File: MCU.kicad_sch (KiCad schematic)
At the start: 46 parts, among them J1 CC Prog/Debug, J2 UART0, J7 Control Outputs, U1 CC1110, U2 MIC803, X1 TG2520SMN 27MHz

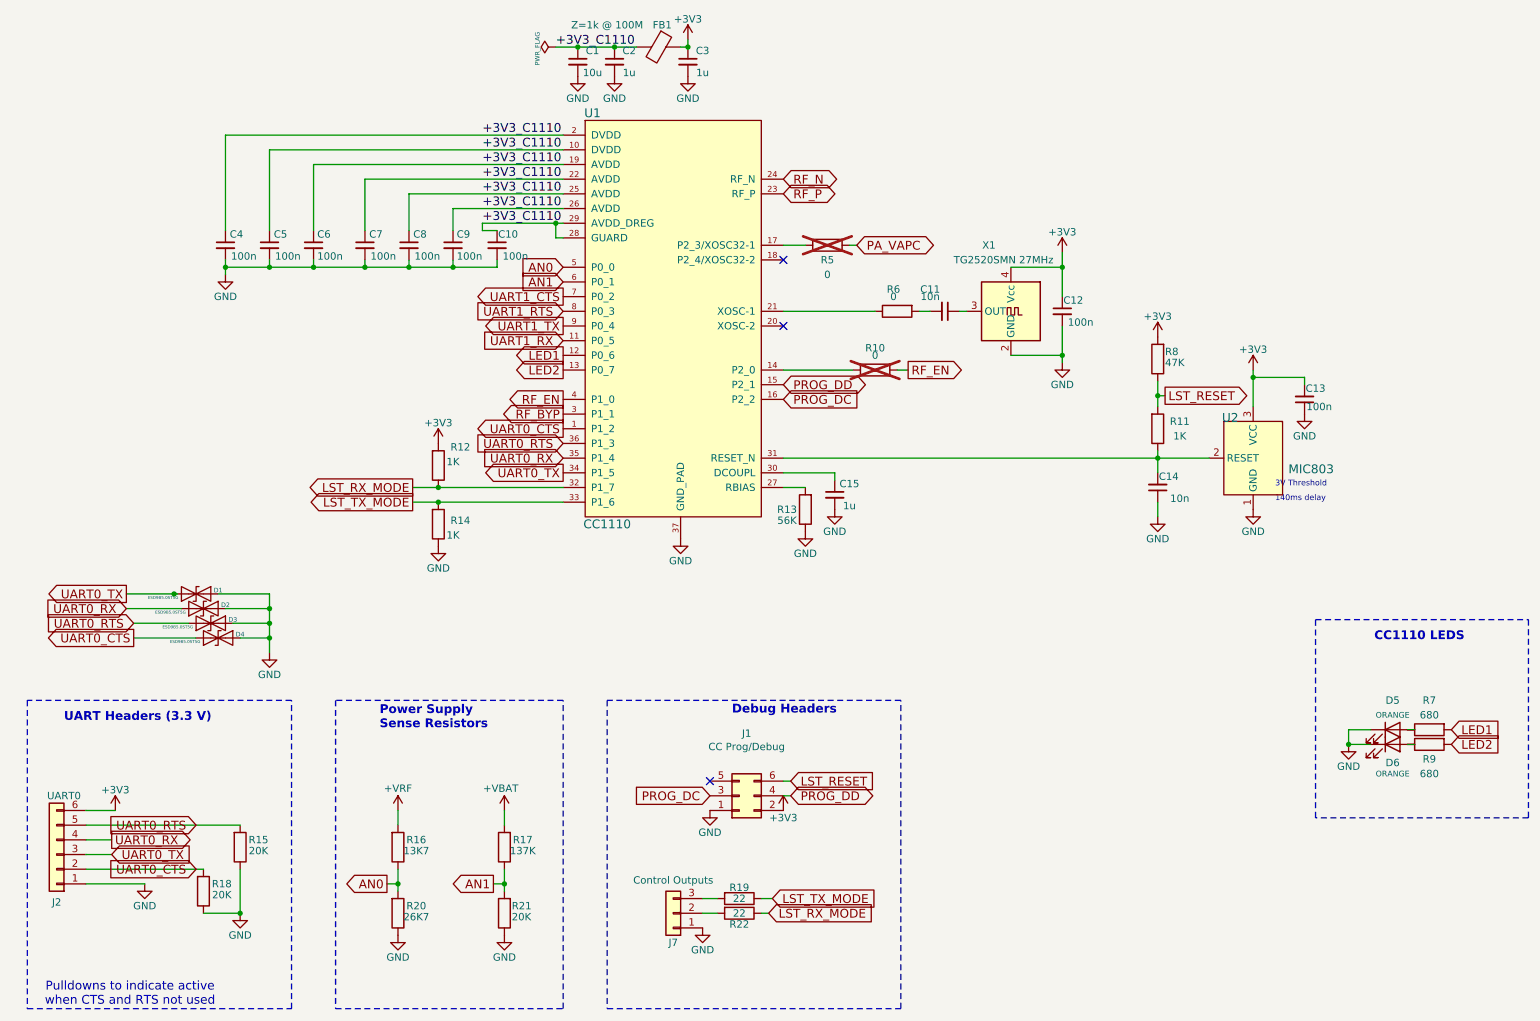
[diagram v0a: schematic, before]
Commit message: automatic schematic and pcb valiadation and cleanup
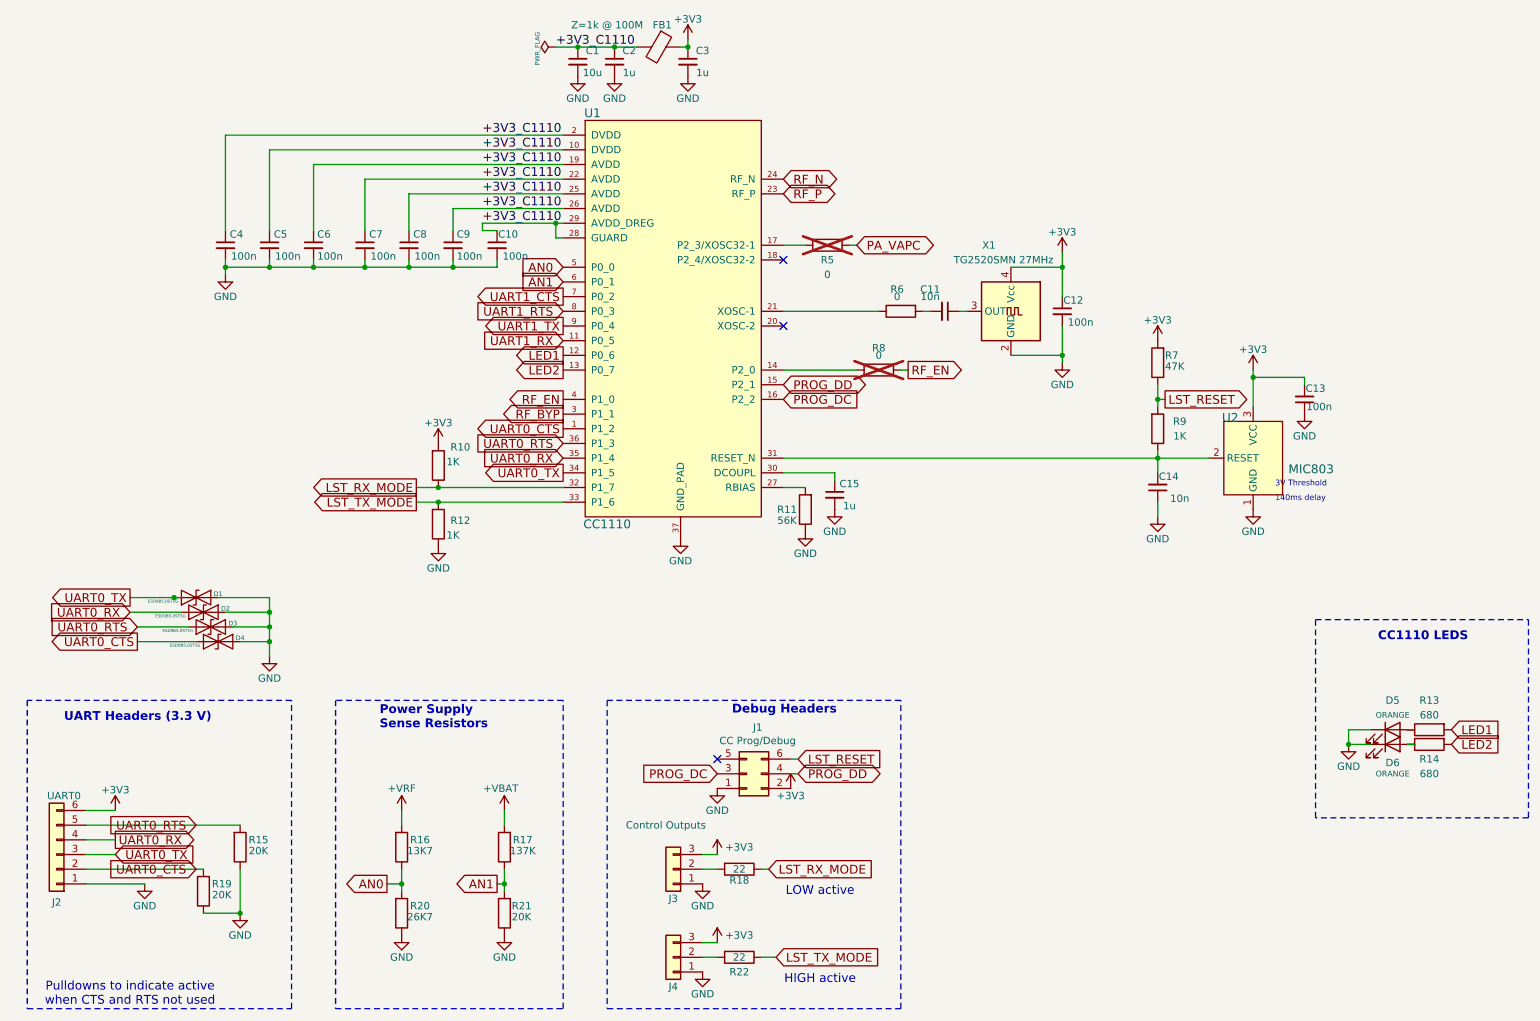
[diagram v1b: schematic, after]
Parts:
- removed R19: 22, Resistor_SMD:R_0603_1608Metric_Pad0.98x0.95mm_HandSolder, symbol Device:R
- added J4: Control Outputs, Connector_PinHeader_2.54mm:PinHeader_1x03_P2.54mm_Vertical, symbol Connector_Generic:Conn_01x03
- added R22: 22, Resistor_SMD:R_0603_1608Metric_Pad0.98x0.95mm_HandSolder, symbol Device:R
- renumbered J7 to J3, R12 to R10, R13 to R11, R14 to R12, R7 to R13, R9 to R14, R22 to R18, R18 to R19, R8 to R7, R10 to R8, R11 to R9
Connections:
- net +3V3: now also J3.3 (Pin_3), J4.3 (Pin_3)
- net GND: now also J4.1 (Pin_1)
- net LST_TX_MODE: now also R22.1
- new net: J4.2 (Pin_2), R22.2
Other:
- note added: "HIGH active"
- note added: "LOW active"
- moved on the sheet: D1, D2, D3, D4, J1, J3, R16, R18, R20, R6, R7, R8

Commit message: temporary branch for radio to pc104
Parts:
- removed D1, D2, D3, D4: ESD9B5.0ST5G, LED_SMD:LED_0603_1608Metric_Pad1.05x0.95mm_HandSolder, symbol Diode:ESD9B5.0ST5G
- added TP1: TestPoint, symbol Connector:TestPoint
- R11: renamed from R15; value 20K -> 100K
- R12: renamed from R16; value 13K7 -> DNP; now not fitted
- R13: renamed from R17; value 137K -> 20K
- R15: renamed from R19; value 20K -> 100K
- R16: renamed from R20; value 26K7 -> DNP; now not fitted
- R17: renamed from R21; value 20K -> 47K
- renumbered D5 to D1, D6 to D2, R5 to R1, R14 to R10, R18 to R14, R22 to R18, R6 to R2, R7 to R3, R8 to R4, R9 to R5, R10 to R6, R11 to R7, R12 to R8, R13 to R9
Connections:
- net UART0_CTS: no longer J2.2 (Pin_2), R15.2
- net UART0_RTS: no longer J2.5 (Pin_5), R11.2
- net UART0_RX: no longer J2.4 (Pin_4)
- net UART0_TX: no longer J2.3 (Pin_3)
- net UART1_CTS: now also J2.2 (Pin_2), R15.2
- net UART1_RTS: now also J2.5 (Pin_5), R11.2
- net UART1_RX: now also J2.4 (Pin_4)
- net UART1_TX: now also J2.3 (Pin_3)
- net +3V3 renamed 3V3
- net +VBAT renamed VRF
- net +VRF: no longer names the net of R12.2
- net +VRF: now also TP1.1
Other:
- moved on the sheet: C3

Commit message: use Common libraries, replace TI MCU with STM32 for CAN bridge
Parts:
- TP1: footprint (none) -> TestPoint:TestPoint_Pad_1.5x1.5mm
- U1: footprint Project:Texas_RHH0036C_VQFN-36-1EP_6x6mm_P0.5mm_EP4.4x4.4mm_ThermalVias -> Common:Texas_RHH0036C_VQFN-36-1EP_6x6mm_P0.5mm_EP4.4x4.4mm_ThermalVias
- X1: value TG2520SMN 27MHz -> 27MHz; footprint Project:Oscillator_SMD_SeikoEpson_TG2520SMN-xxx-xxxxxx-4Pin_2.5x2.0mm -> Oscillator:Oscillator_SMD_Abracon_ASDMB-4Pin_2.5x2.0mm; Mfr. # TG2520SMN 27.0000M-MCGNNM3 -> ASDAIG-27.000MHZ-C-S-T
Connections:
- net UART0_CTS: now also J2.2 (Pin_2), R15.2
- net UART0_RTS: now also J2.5 (Pin_5), R11.2
- net UART0_RX: now also J2.4 (Pin_4)
- net UART0_TX: now also J2.3 (Pin_3)
- net UART1_CTS: no longer J2.2 (Pin_2), R15.2
- net UART1_RTS: no longer J2.5 (Pin_5), R11.2
- net UART1_RX: no longer J2.4 (Pin_4)
- net UART1_TX: no longer J2.3 (Pin_3)
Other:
- note added: "UART0 Headers (3.3 V)"
- note removed: "UART Headers (3.3 V)"
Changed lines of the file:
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@@
 		)
 	)
-	(text "UART Headers (3.3 V)"
+	(text "UART0 Headers (3.3 V)"
 		(exclude_from_sim no)
 		(at 27.94 146.05 0)
@@
 		)
 	)
-	(label "UART1_TX"
-		(at 114.3 77.47 180)
-		(fields_autoplaced yes)
-		(effects
-			(font
-				(size 1.524 1.524)
-			)
-			(justify right bottom)
-		)
-	)
 	(label "+3V3_C1110"
 		(at 114.3 59.69 180)
@@
 		)
 	)
-	(label "UART1_CTS"
+	(label "UART0_CTS"
 		(at 50.8 171.45 180)
 		(fields_autoplaced yes)
@@
 		)
 	)
-	(label "UART1_RX"
+	(label "UART0_RX"
 		(at 38.1 166.37 0)
 		(fields_autoplaced yes)
@@
 		)
 	)
-	(label "UART1_RTS"
-		(at 114.3 74.93 180)
+	(label "LED1"
+		(at 114.3 82.55 180)
 		(fields_autoplaced yes)
 		(effects
@@
 		)
 	)
-	(label "LED1"
-		(at 114.3 82.55 180)
+	(label "+3V3_C1110"
+		(at 113.03 29.21 0)
 		(fields_autoplaced yes)
 		(effects
@@
 				(size 1.524 1.524)
 			)
-			(justify right bottom)
+			(justify left bottom)
 		)
 	)
-	(label "UART1_RX"
-		(at 114.3 80.01 180)
+	(label "UART0_RX"
+		(at 114.3 100.33 180)
 		(fields_autoplaced yes)
 		(effects
@@
 		)
 	)
-	(label "+3V3_C1110"
-		(at 113.03 29.21 0)
+	(label "LST_TX_MODE"
+		(at 151.13 186.69 0)
 		(fields_autoplaced yes)
 		(effects
@@
 		)
 	)
-	(label "LST_TX_MODE"
-		(at 151.13 186.69 0)
+	(label "+3V3_C1110"
+		(at 99.695 46.99 0)
 		(fields_autoplaced yes)
 		(effects
@@
 		)
 	)
-	(label "+3V3_C1110"
-		(at 99.695 46.99 0)
+	(label "UART0_CTS"
+		(at 114.3 95.25 180)
 		(fields_autoplaced yes)
 		(effects
@@
 				(size 1.524 1.524)
 			)
-			(justify left bottom)
+			(justify right bottom)
 		)
 	)
-	(label "UART1_TX"
+	(label "UART0_TX"
 		(at 38.1 168.91 0)
 		(fields_autoplaced yes)
@@
 		)
 	)
-	(label "UART1_RTS"
+	(label "UART0_RTS"
 		(at 50.8 163.83 180)
 		(fields_autoplaced yes)
@@
 		)
 	)
-	(label "UART1_CTS"
-		(at 114.3 72.39 180)
+	(label "UART0_RTS"
+		(at 114.3 97.79 180)
+		(fields_autoplaced yes)
+		(effects
+			(font
+				(size 1.524 1.524)
+			)
+			(justify right bottom)
+		)
+	)
+	(label "UART0_TX"
+		(at 114.3 102.87 180)
 		(fields_autoplaced yes)
 		(effects
@@
 		)
 	)
-	(hierarchical_label "UART0_TX"
-		(shape output)
-		(at 114.3 102.87 180)
-		(fields_autoplaced yes)
-		(effects
-			(font
-				(size 1.524 1.524)
-			)
-			(justify right)
-		)
-	)
 	(hierarchical_label "3V3"
 		(shape input)
@@
 		)
 	)
-	(hierarchical_label "UART0_CTS"
-		(shape output)
-		(at 114.3 95.25 180)
-		(fields_autoplaced yes)
-		(effects
-			(font
-				(size 1.524 1.524)
-			)
-			(justify right)
-		)
-	)
 	(hierarchical_label "LST_RX_MODE"
 		(shape output)
@@
 		)
 	)
-	(hierarchical_label "UART0_RX"
-		(shape input)
-		(at 114.3 100.33 180)
-		(fields_autoplaced yes)
-		(effects
-			(font
-				(size 1.524 1.524)
-			)
-			(justify right)
-		)
-	)
 	(hierarchical_label "VRF"
 		(shape input)
@@
 		)
 	)
-	(hierarchical_label "GND"
+	(hierarchical_label "UART1_TX"
 		(shape input)
-		(at 233.68 110.49 0)
+		(at 114.3 77.47 180)
 		(fields_autoplaced yes)
 		(effects
@@
 				(size 1.524 1.524)
 			)
-			(justify left)
+			(justify right)
 		)
 	)
-	(hierarchical_label "UART0_RTS"
+	(hierarchical_label "GND"
 		(shape input)
-		(at 114.3 97.79 180)
+		(at 233.68 110.49 0)
 		(fields_autoplaced yes)
 		(effects
@@
 				(size 1.524 1.524)
 			)
-			(justify right)
+			(justify left)
 		)
 	)
@@
 		)
 	)
+	(hierarchical_label "UART1_RTS"
+		(shape input)
+		(at 114.3 74.93 180)
+		(fields_autoplaced yes)
+		(effects
+			(font
+				(size 1.524 1.524)
+			)
+			(justify right)
+		)
+	)
 	(hierarchical_label "3V3"
 		(shape input)
@@
 		)
 	)
+	(hierarchical_label "UART1_RX"
+		(shape input)
+		(at 114.3 80.01 180)
+		(fields_autoplaced yes)
+		(effects
+			(font
+				(size 1.524 1.524)
+			)
+			(justify right)
+		)
+	)
 	(hierarchical_label "3V3"
 		(shape input)
@@
 		)
 	)
+	(hierarchical_label "UART1_CTS"
+		(shape input)
+		(at 114.3 72.39 180)
+		(fields_autoplaced yes)
+		(effects
+			(font
+				(size 1.524 1.524)
+			)
+			(justify right)
+		)
+	)
 	(hierarchical_label "RF_EN"
 		(shape output)
@@
 			)
 		)
-		(property "Value" "TG2520SMN 27MHz"
+		(property "Value" "27MHz"
 			(at 190.5 66.04 0)
 			(effects
@@
 			)
 		)
-		(property "Footprint" "Project:Oscillator_SMD_SeikoEpson_TG2520SMN-xxx-xxxxxx-4Pin_2.5x2.0mm"
+		(property "Footprint" "Oscillator:Oscillator_SMD_Abracon_ASDMB-4Pin_2.5x2.0mm"
 			(at 180.34 83.82 0)
 			(effects
@@
 			)
 		)
-		(property "Datasheet" "https://support.epson.biz/td/api/doc_check.php?dl=app_TG2520SMN&lang=en"
+		(property "Datasheet" "https://abracon.com/AIGOscillators/ASDAIG.pdf"
 			(at 194.31 74.93 0)
 			(effects
@@
 			)
 		)
-		(property "Description" "Crystal Oscillator Low Profile / High Stability TCXO"
+		(property "Description" "Crystal Oscillator 27MHz"
 			(at 191.77 74.93 0)
 			(effects
@@
 			)
 		)
-		(property "Mfr. #" "TG2520SMN 27.0000M-MCGNNM3"
+		(property "Mfr. #" "ASDAIG-27.000MHZ-C-S-T"
 			(at 191.77 66.6496 0)
 			(effects
@@
 			)
 		)
-		(property "Footprint" "Project:Texas_RHH0036C_VQFN-36-1EP_6x6mm_P0.5mm_EP4.4x4.4mm_ThermalVias"
+		(property "Footprint" "Common:Texas_RHH0036C_VQFN-36-1EP_6x6mm_P0.5mm_EP4.4x4.4mm_ThermalVias"
 			(at 138.43 90.17 0)
 			(effects
@@
 		(on_board yes)
 		(dnp no)
-		(property "Reference" "#FLG01"
+		(property "Reference" "#FLG05"
 			(at 111.125 29.21 0)
 			(effects
@@
 			(project "openlst-hw"
 				(path "/a863a5ec-a5d4-4f54-be53-e8c01d5e3ac4/f5534efb-fc6e-465a-a57b-daca63f2ce0c"
-					(reference "#FLG01")
+					(reference "#FLG05")
 					(unit 1)
 				)
@@
 			)
 		)
-		(property "Footprint" ""
+		(property "Footprint" "TestPoint:TestPoint_Pad_1.5x1.5mm"
 			(at 91.44 161.29 0)
 			(effects
@@
 		(on_board yes)
 		(dnp no)
-		(property "Reference" "#PWR06"
+		(property "Reference" "#PWR02"
 			(at 250.19 156.21 0)
 			(effects
@@
 			(project "openlst-hw"
 				(path "/a863a5ec-a5d4-4f54-be53-e8c01d5e3ac4/f5534efb-fc6e-465a-a57b-daca63f2ce0c"
-					(reference "#PWR06")
+					(reference "#PWR02")
 					(unit 1)
 				)
